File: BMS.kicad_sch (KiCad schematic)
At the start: 136 parts, among them J1 TopConn, J10 BMS1OTP, J11 BMS2OTP, J2 BottomConn, J6 TopConn, U10 TLP185, U11 ISO1640BDR, U12 TLP185, U4 BQ7695201PFBR, U8 ISO1640BDR

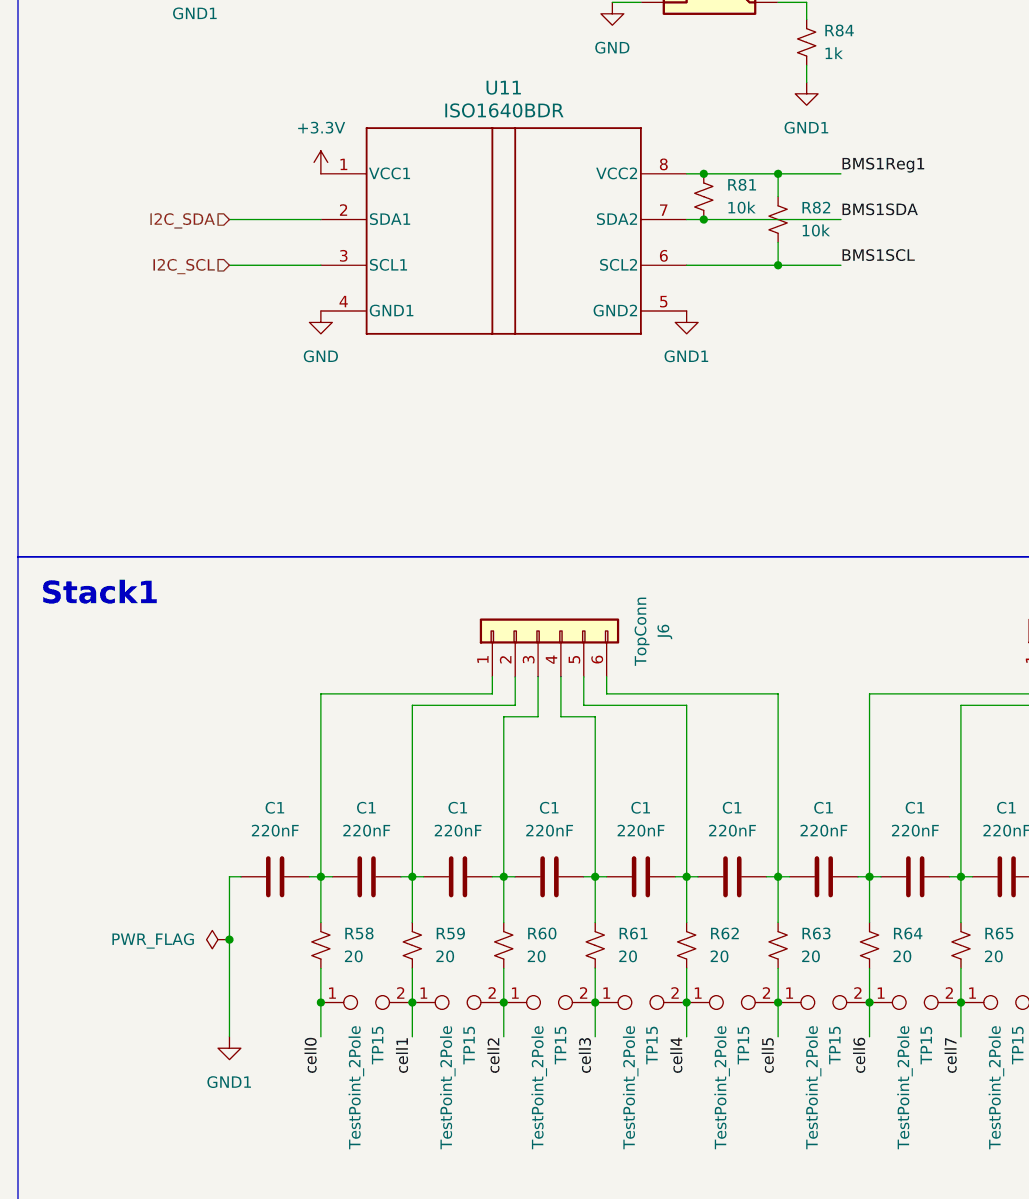
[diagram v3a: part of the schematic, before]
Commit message: power flags
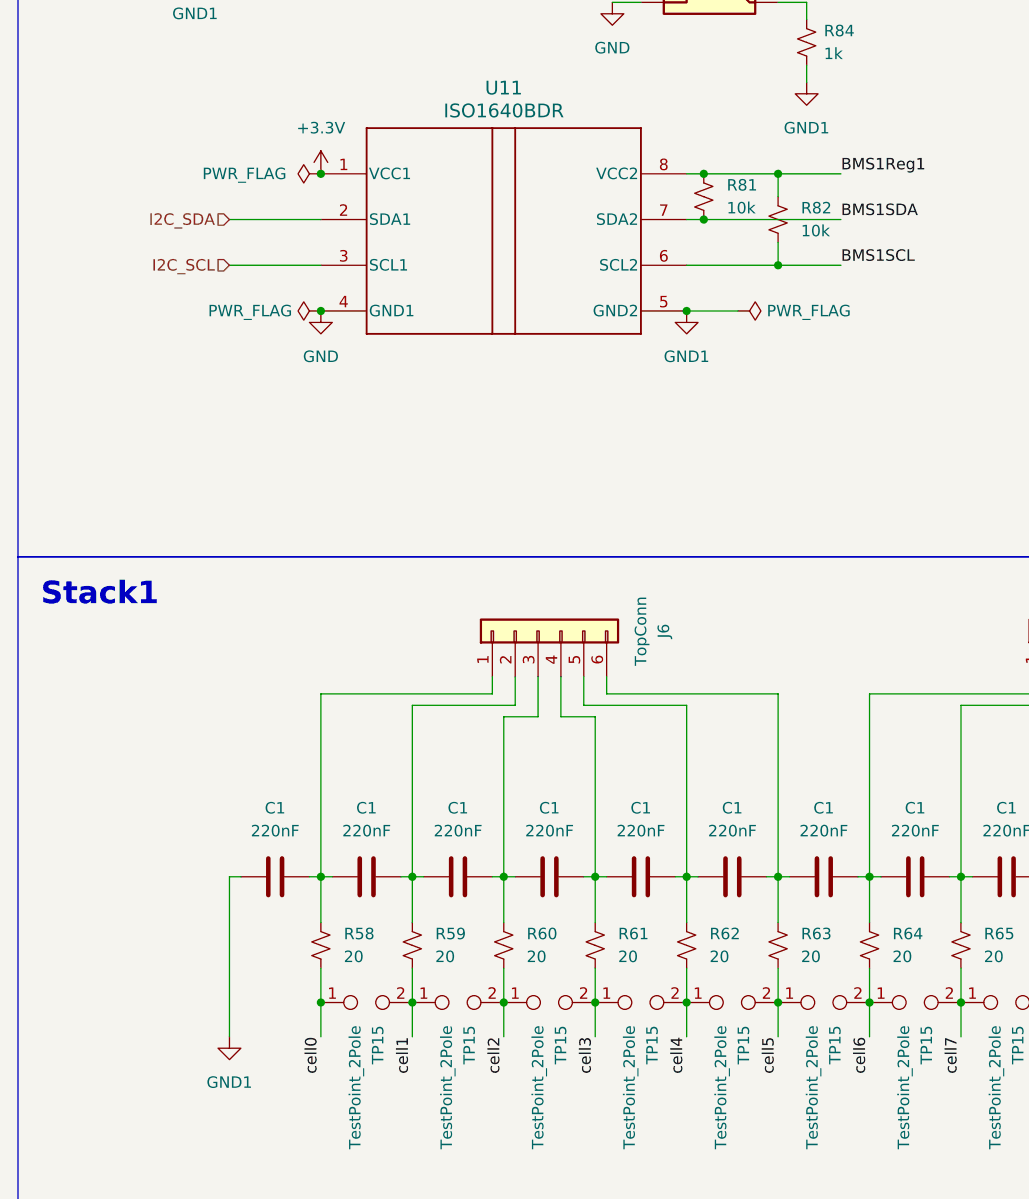
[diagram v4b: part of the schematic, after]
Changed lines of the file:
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@@
   (junction (at 76.2 220.98) (diameter 0) (color 0 0 0 0)
   )
+  (junction (at 86.36 144.145) (diameter 0) (color 0 0 0 0)
+  )
   (junction (at 208.28 187.96) (diameter 0) (color 0 0 0 0)
   )
@@
   (junction (at 282.575 69.215) (diameter 0) (color 0 0 0 0)
   )
+  (junction (at 45.72 128.905) (diameter 0) (color 0 0 0 0)
+  )
   (junction (at 299.72 207.01) (diameter 0) (color 0 0 0 0)
   )
@@
   (junction (at 218.44 220.98) (diameter 0) (color 0 0 0 0)
   )
+  (junction (at 45.72 144.145) (diameter 0) (color 0 0 0 0)
+  )
   (junction (at 350.52 207.01) (diameter 0) (color 0 0 0 0)
   )
@@
   (junction (at 279.4 207.01) (diameter 0) (color 0 0 0 0)
   )
-  (junction (at 35.56 213.995) (diameter 0) (color 0 0 0 0)
-  )
   (junction (at 248.92 207.01) (diameter 0) (color 0 0 0 0)
   )
@@
     (stroke (width 0) (type default))
   )
-  (wire (pts (xy 35.56 207.01) (xy 35.56 213.995))
-    (stroke (width 0) (type default))
-  )
   (wire (pts (xy 373.38 67.945) (xy 373.38 64.77))
     (stroke (width 0) (type default))
@@
     (stroke (width 0) (type default))
   )
-  (wire (pts (xy 35.56 213.995) (xy 35.56 224.79))
+  (wire (pts (xy 35.56 207.01) (xy 35.56 224.79))
     (stroke (width 0) (type default))
   )
@@
     (stroke (width 0) (type default))
   )
+  (wire (pts (xy 92.075 144.145) (xy 86.36 144.145))
+    (stroke (width 0) (type default))
+  )
   (wire (pts (xy 321.31 186.69) (xy 340.36 186.69))
     (stroke (width 0) (type default))
@@
     )
   )
+  (symbol (lib_id "power:PWR_FLAG") (at 45.72 128.905 90) (unit 1)
+    (in_bom yes) (on_board yes) (dnp no) (fields_autoplaced)
+    (property "Reference" "#FLG03" (at 43.815 128.905 0)
+      (effects (font (size 1.27 1.27)) hide)
+    )
+    (property "Value" "PWR_FLAG" (at 41.91 128.905 90)
+      (effects (font (size 1.27 1.27)) (justify left))
+    )
+    (property "Footprint" "" (at 45.72 128.905 0)
+      (effects (font (size 1.27 1.27)) hide)
+    )
+    (property "Datasheet" "~" (at 45.72 128.905 0)
+      (effects (font (size 1.27 1.27)) hide)
+    )
+    (pin "1")
+    (instances
+      (project "BPS-Minion"
+        (path "/86f4c077-2357-4bc0-9102-0d9b954ffb24/f4179d79-1229-45f6-9801-99c07e86bfe4"
+          (reference "#FLG03") (unit 1)
+        )
+      )
+    )
+  )
   (symbol (lib_id "power:+3.3V") (at 318.77 104.14 0) (unit 1)
     (in_bom yes) (on_board yes) (dnp no) (fields_autoplaced)
@@
     )
   )
-  (symbol (lib_id "power:PWR_FLAG") (at 35.56 213.995 90) (unit 1)
-    (in_bom yes) (on_board yes) (dnp no) (fields_autoplaced)
-    (property "Reference" "#FLG04" (at 33.655 213.995 0)
-      (effects (font (size 1.27 1.27)) hide)
-    )
-    (property "Value" "PWR_FLAG" (at 31.75 213.995 90)
-      (effects (font (size 1.27 1.27)) (justify left))
-    )
-    (property "Footprint" "" (at 35.56 213.995 0)
-      (effects (font (size 1.27 1.27)) hide)
-    )
-    (property "Datasheet" "~" (at 35.56 213.995 0)
-      (effects (font (size 1.27 1.27)) hide)
-    )
-    (pin "1")
-    (instances
-      (project "BPS-Minion"
-        (path "/86f4c077-2357-4bc0-9102-0d9b954ffb24"
-          (reference "#FLG04") (unit 1)
-        )
-        (path "/86f4c077-2357-4bc0-9102-0d9b954ffb24/f4179d79-1229-45f6-9801-99c07e86bfe4"
-          (reference "#FLG02") (unit 1)
-        )
-      )
-    )
-  )
   (symbol (lib_id "Connector:TestPoint_2Pole") (at 50.8 220.98 0) (unit 1)
     (in_bom yes) (on_board yes) (dnp no)
@@
         )
       )
+    )
+  )
+  (symbol (lib_id "power:PWR_FLAG") (at 45.72 144.145 90) (unit 1)
+    (in_bom yes) (on_board yes) (dnp no) (fields_autoplaced)
+    (property "Reference" "#FLG04" (at 43.815 144.145 0)
+      (effects (font (size 1.27 1.27)) hide)
+    )
+    (property "Value" "PWR_FLAG" (at 42.545 144.145 90)
+      (effects (font (size 1.27 1.27)) (justify left))
+    )
+    (property "Footprint" "" (at 45.72 144.145 0)
+      (effects (font (size 1.27 1.27)) hide)
+    )
+    (property "Datasheet" "~" (at 45.72 144.145 0)
+      (effects (font (size 1.27 1.27)) hide)
+    )
+    (pin "1")
+    (instances
+      (project "BPS-Minion"
+        (path "/86f4c077-2357-4bc0-9102-0d9b954ffb24/f4179d79-1229-45f6-9801-99c07e86bfe4"
+          (reference "#FLG04") (unit 1)
+        )
+      )
+    )
+  )
+  (symbol (lib_id "power:PWR_FLAG") (at 92.075 144.145 270) (unit 1)
+    (in_bom yes) (on_board yes) (dnp no) (fields_autoplaced)
+    (property "Reference" "#FLG01" (at 93.98 144.145 0)
+      (effects (font (size 1.27 1.27)) hide)
+    )
+    (property "Value" "PWR_FLAG" (at 95.25 144.145 90)
+      (effects (font (size 1.27 1.27)) (justify left))
+    )
+    (property "Footprint" "" (at 92.075 144.145 0)
+      (effects (font (size 1.27 1.27)) hide)
+    )
+    (property "Datasheet" "~" (at 92.075 144.145 0)
+      (effects (font (size 1.27 1.27)) hide)
+    )
+    (pin "1")
+    (instances
+      (project "BPS-Minion"
+        (path "/86f4c077-2357-4bc0-9102-0d9b954ffb24/f4179d79-1229-45f6-9801-99c07e86bfe4"
+          (reference "#FLG01") (unit 1)
+        )
+      )

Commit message: lakshay changes:
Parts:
- R84: value 1k -> 10k
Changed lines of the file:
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@@
       (effects (font (size 1.27 1.27)) (justify right))
     )
-    (property "Value" "1k" (at 101.6 115.57 0)
+    (property "Value" "10k" (at 101.6 115.57 0)
       (effects (font (size 1.27 1.27)) (justify right))
     )

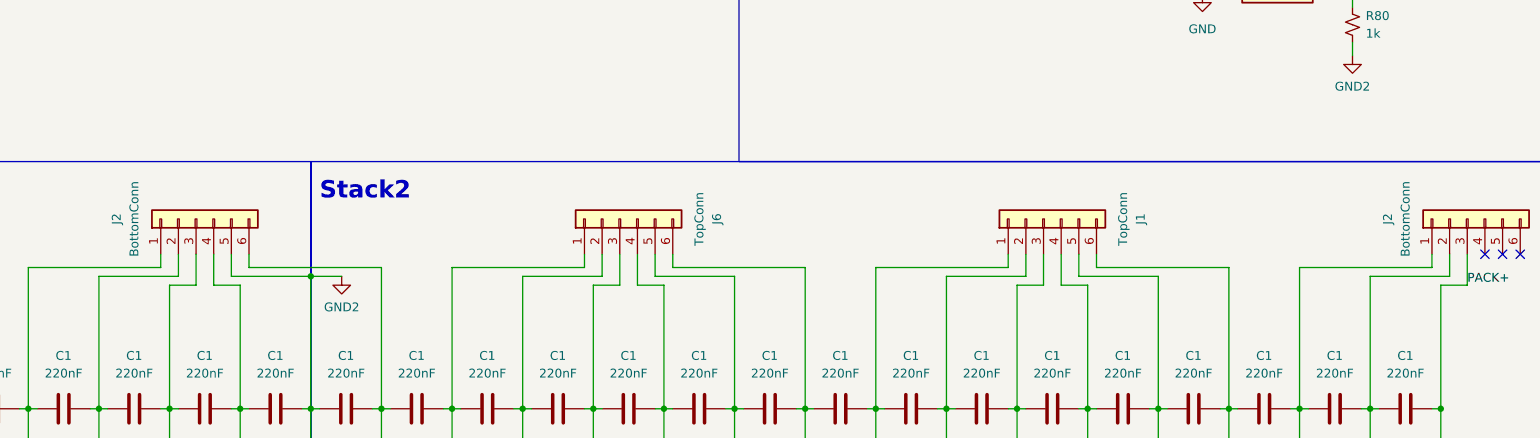
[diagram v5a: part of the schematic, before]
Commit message: define edge cuts for new volttemp
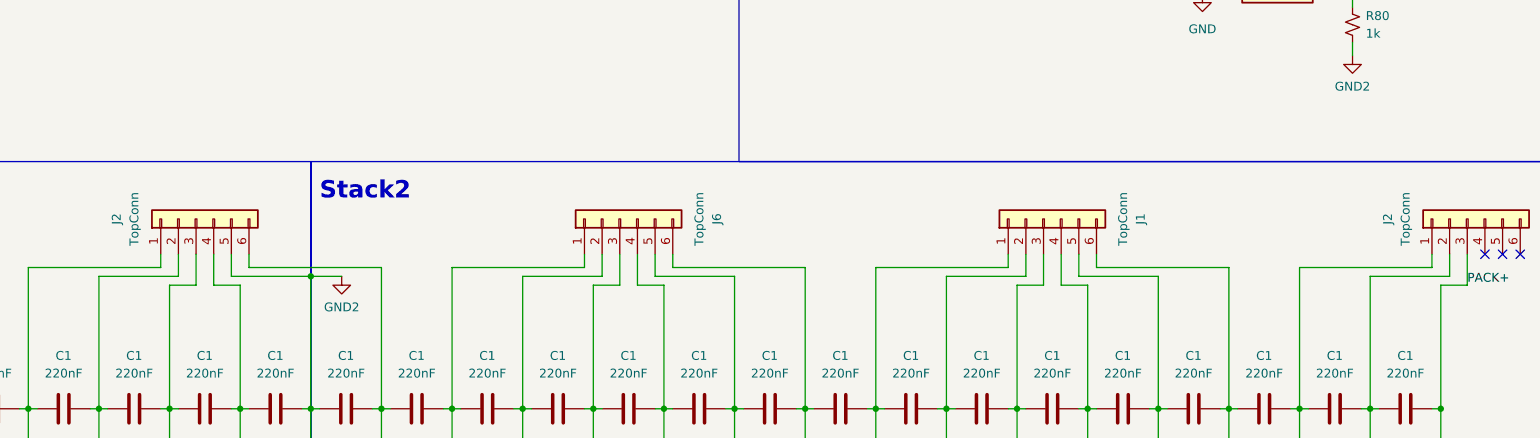
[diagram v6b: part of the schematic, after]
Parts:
- J1, J6: footprint Connector_Molex:Molex_Micro-Fit_3.0_43650-0700_1x07_P3.00mm_Horizontal -> Connector_Molex:Molex_Micro-Fit_3.0_43650-0600_1x06_P3.00mm_Horizontal
- J2: value BottomConn -> TopConn; footprint Connector_Molex:Molex_Micro-Fit_3.0_43650-0700_1x07_P3.00mm_Horizontal -> Connector_Molex:Molex_Micro-Fit_3.0_43650-0600_1x06_P3.00mm_Horizontal
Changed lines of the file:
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@@
       (effects (font (size 1.27 1.27)))
     )
-    (property "Value" "BottomConn" (at 182.88 179.705 0)
-      (effects (font (size 1.27 1.27)))
-    )
-    (property "Footprint" "Connector_Molex:Molex_Micro-Fit_3.0_43650-0700_1x07_P3.00mm_Horizontal" (at 191.77 179.705 0)
+    (property "Value" "TopConn" (at 182.88 179.705 0)
+      (effects (font (size 1.27 1.27)))
+    )
+    (property "Footprint" "Connector_Molex:Molex_Micro-Fit_3.0_43650-0600_1x06_P3.00mm_Horizontal" (at 191.77 179.705 0)
       (effects (font (size 1.27 1.27)) hide)
     )
@@
       (effects (font (size 1.27 1.27)))
     )
-    (property "Footprint" "Connector_Molex:Molex_Micro-Fit_3.0_43650-0700_1x07_P3.00mm_Horizontal" (at 252.73 179.705 0)
+    (property "Footprint" "Connector_Molex:Molex_Micro-Fit_3.0_43650-0600_1x06_P3.00mm_Horizontal" (at 252.73 179.705 0)
       (effects (font (size 1.27 1.27)) hide)
     )
@@
       (effects (font (size 1.27 1.27)))
     )
-    (property "Footprint" "Connector_Molex:Molex_Micro-Fit_3.0_43650-0700_1x07_P3.00mm_Horizontal" (at 69.85 179.705 0)
+    (property "Footprint" "Connector_Molex:Molex_Micro-Fit_3.0_43650-0600_1x06_P3.00mm_Horizontal" (at 69.85 179.705 0)
       (effects (font (size 1.27 1.27)) hide)
     )
@@
       (effects (font (size 1.27 1.27)))
     )
-    (property "Footprint" "Connector_Molex:Molex_Micro-Fit_3.0_43650-0700_1x07_P3.00mm_Horizontal" (at 313.69 179.705 0)
+    (property "Footprint" "Connector_Molex:Molex_Micro-Fit_3.0_43650-0600_1x06_P3.00mm_Horizontal" (at 313.69 179.705 0)
       (effects (font (size 1.27 1.27)) hide)
     )
@@
       (effects (font (size 1.27 1.27)))
     )
-    (property "Footprint" "Connector_Molex:Molex_Micro-Fit_3.0_43650-0700_1x07_P3.00mm_Horizontal" (at 130.81 179.705 0)
+    (property "Footprint" "Connector_Molex:Molex_Micro-Fit_3.0_43650-0600_1x06_P3.00mm_Horizontal" (at 130.81 179.705 0)
       (effects (font (size 1.27 1.27)) hide)
     )
@@
       (effects (font (size 1.27 1.27)))
     )
-    (property "Value" "BottomConn" (at 365.76 179.705 0)
-      (effects (font (size 1.27 1.27)))
-    )
-    (property "Footprint" "Connector_Molex:Molex_Micro-Fit_3.0_43650-0700_1x07_P3.00mm_Horizontal" (at 374.65 179.705 0)
-      (effects (font (size 1.27 1.27)) hide)
-    )
+    (property "Value" "TopConn" (at 365.76 179.705 0)
+      (effects (font (size 1.27 1.27)))
+    )
+    (property "Footprint" "Connector_Molex:Molex_Micro-Fit_3.0_43650-0600_1x06_P3.00mm_Horizontal" (at 374.65 179.705 0)
+      (effects (font (size 1.27 1.27)) hide)
+    )

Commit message: why so many bugs >:(
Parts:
- removed C1 (x33): 220nF, Capacitor_SMD:C_0805_2012Metric_Pad1.18x1.45mm_HandSolder, symbol Device:C
- removed D1 (x2): BAS16W, Package_TO_SOT_SMD:SOT-323_SC-70, symbol Diode:BAS16W
- removed J1 (x2), J2 (x2), J6 (x2): TopConn, Connector_Molex:Molex_Micro-Fit_3.0_43650-0600_1x06_P3.00mm_Horizontal, symbol Connector_Generic:Conn_01x06
- removed R1, R10, R11, R12, R13, R14, R15, R16, R2, R3, R4, R5, R58, R59, R6, R60, R61, R62, R63, R64, R65, R66, R67, R68, R69, R7, R70, R71, R72, R73, R74, R8, R9: 20, Resistor_SMD:R_0805_2012Metric, symbol Device:R_Small_US
- removed TP15 (x32): TestPoint_2Pole, Jumper:SolderJumper-2_P1.3mm_Open_RoundedPad1.0x1.5mm, symbol Connector:TestPoint_2Pole
- removed U10, U12: TLP185, Package_SO:SOIC-4_4.55x3.7mm_P2.54mm, symbol Isolator:TLP185
- added C2 (x4): 1u, Capacitor_SMD:C_0805_2012Metric_Pad1.18x1.45mm_HandSolder, symbol Device:C
- added D2, D3: 1N4448W, Diode_SMD:D_SOD-123, symbol Diode:1N4448W
- added U1 (x2): EL3H7, Package_SO:SOP-4_4.4x2.6mm_P1.27mm, symbol Isolator:EL817
- renumbered J10 to J2, J11 to J3, R79 to R10, R80 to R13, R77 to R14, R78 to R15, R83 to R3, R81 to R4, R82 to R7, R84 to R8, U11 to U3, U8 to U6
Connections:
- net cell16 is gone; now on net GND2: U4.16 (VC0), U4.48 (VC16)
- net +3.3V: now also C2.2, C2.2
- net BMS1Reg1: now also C2.1, U1.4
- net BMS1Reset: now also U1.3
- net BMS2Reg1: now also C2.1, U1.4
- net BMS2Reset: now also U1.3
- net GND: now also C2.1, C2.1, U1.2, U1.2
- net GND1: now also C2.2
- net GND2: now also C2.2, D2.2 (A)
- net cell27: no longer U4.4 (VC12)
- net cell28: now also U4.4 (VC12); no longer U4.3 (VC13)
- net cell29: now also U4.3 (VC13); no longer U4.2 (VC14)
- net cell30: now also U4.2 (VC14); no longer U4.1 (VC15)
- net cell31: now also U4.1 (VC15); no longer U4.48 (VC16)
- net cell32: now also U4.48 (VC16), D3.2 (A)
- net at R10.2: now also U1.1
- net at R3.2: now also U1.1
- net at R20.2: now also D2.1 (K)
- net at R20.2: now also D3.1 (K)
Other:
- added sheet BatteryConnector1 (BatteryConnector.kicad_sch)
- added sheet BatteryConnector2 (BatteryConnector.kicad_sch)
- added sheet BatteryConnector3 (BatteryConnector.kicad_sch)
- added sheet BatteryConnector4 (BatteryConnector.kicad_sch)
- added sheet BatteryConnector5 (BatteryConnector.kicad_sch)
- added sheet BatteryConnector6 (BatteryConnector.kicad_sch)

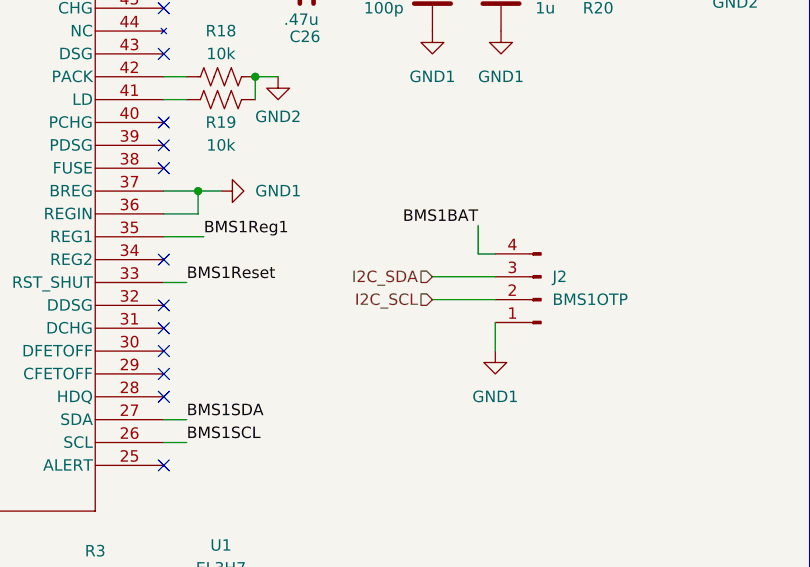
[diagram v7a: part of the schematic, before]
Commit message: Fixed minor bugs with BMS and temp chips
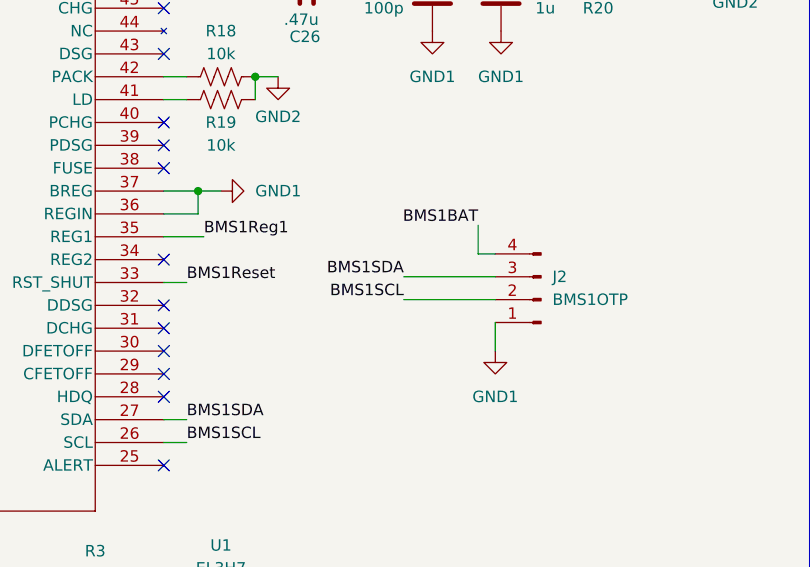
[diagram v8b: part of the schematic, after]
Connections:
- net BMS1SCL: now also J2.2 (Pin_2)
- net BMS1SDA: now also J2.3 (Pin_3)
- net I2C_SCL: no longer J2.2 (Pin_2)
- net I2C_SDA: no longer J2.3 (Pin_3)
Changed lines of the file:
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@@
     (stroke (width 0) (type default))
   )
-  (wire (pts (xy 112.395 71.12) (xy 119.38 71.12))
+  (wire (pts (xy 109.22 71.12) (xy 119.38 71.12))
     (stroke (width 0) (type default))
   )
@@
     (stroke (width 0) (type default))
   )
-  (wire (pts (xy 112.395 68.58) (xy 119.38 68.58))
-    (stroke (width 0) (type default))
-  )
   (wire (pts (xy 196.85 220.345) (xy 200.66 220.345))
     (stroke (width 0) (type default))
@@
   )
   (wire (pts (xy 196.85 212.725) (xy 200.66 212.725))
+    (stroke (width 0) (type default))
+  )
+  (wire (pts (xy 109.22 68.58) (xy 119.38 68.58))
     (stroke (width 0) (type default))
   )
@@
     (effects (font (size 1.27 1.27)) (justify left bottom))
   )
+  (label "BMS1SDA" (at 109.22 68.58 180) (fields_autoplaced)
+    (effects (font (size 1.27 1.27)) (justify right bottom))
+  )
   (label "BMS2Reg1" (at 342.265 59.055 0) (fields_autoplaced)
     (effects (font (size 1.27 1.27)) (justify left bottom))
@@
     (effects (font (size 1.27 1.27)) (justify left bottom))
   )
+  (label "BMS1SCL" (at 109.22 71.12 180) (fields_autoplaced)
+    (effects (font (size 1.27 1.27)) (justify right bottom))
+  )
   (label "BMS1SCL" (at 85.09 86.995 0) (fields_autoplaced)
     (effects (font (size 1.27 1.27)) (justify left bottom))
@@
     (effects (font (size 1.27 1.27)) (justify right))
   )
-  (hierarchical_label "I2C_SCL" (shape input) (at 112.395 71.12 180) (fields_autoplaced)
-    (effects (font (size 1.27 1.27)) (justify right))
-  )
   (hierarchical_label "I2C_SCL" (shape input) (at 43.18 139.065 180) (fields_autoplaced)
     (effects (font (size 1.27 1.27)) (justify right))
@@
     (effects (font (size 1.27 1.27)) (justify right))
   )
-  (hierarchical_label "I2C_SDA" (shape input) (at 112.395 68.58 180) (fields_autoplaced)
-    (effects (font (size 1.27 1.27)) (justify right))
-  )
